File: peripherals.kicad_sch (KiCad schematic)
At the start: 21 parts, among them IC5 MAX11613EUA+T, Q3 BSD235NH6327XTSA1, Q4 BSD235NH6327XTSA1

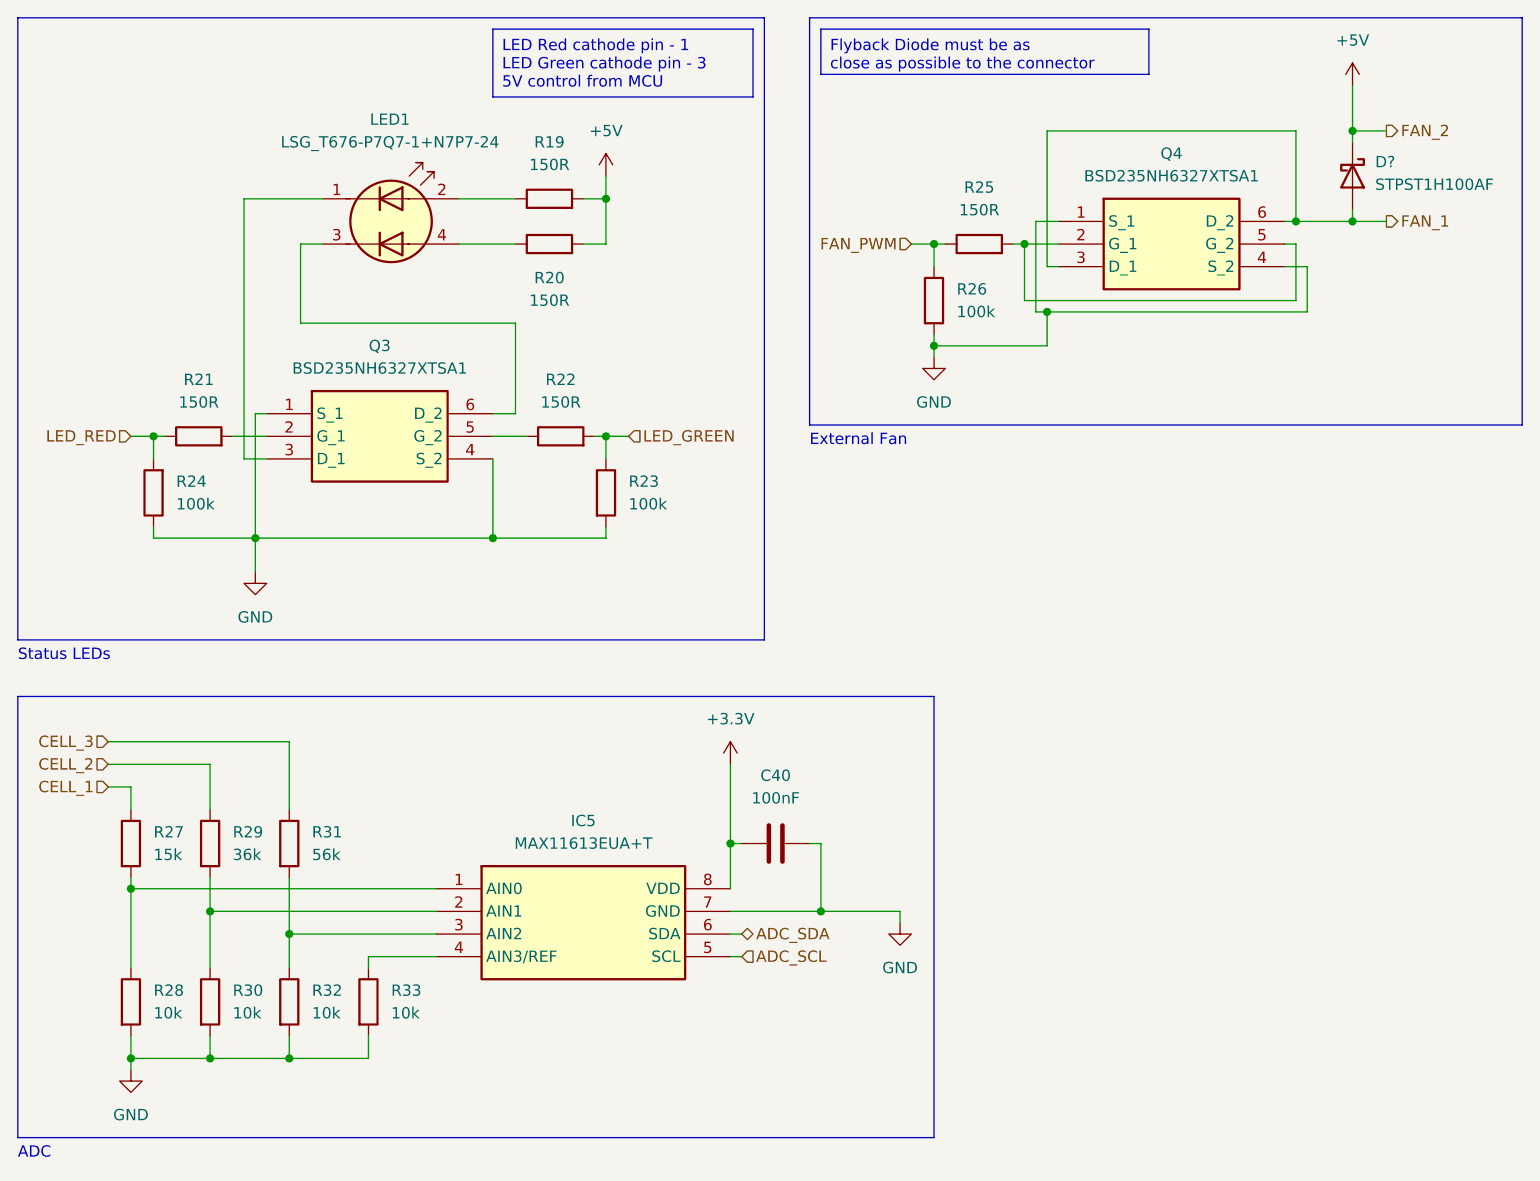
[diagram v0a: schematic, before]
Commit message: New complete schematic version
May need to resize the resistors, also need to change the caps back to electrolytic
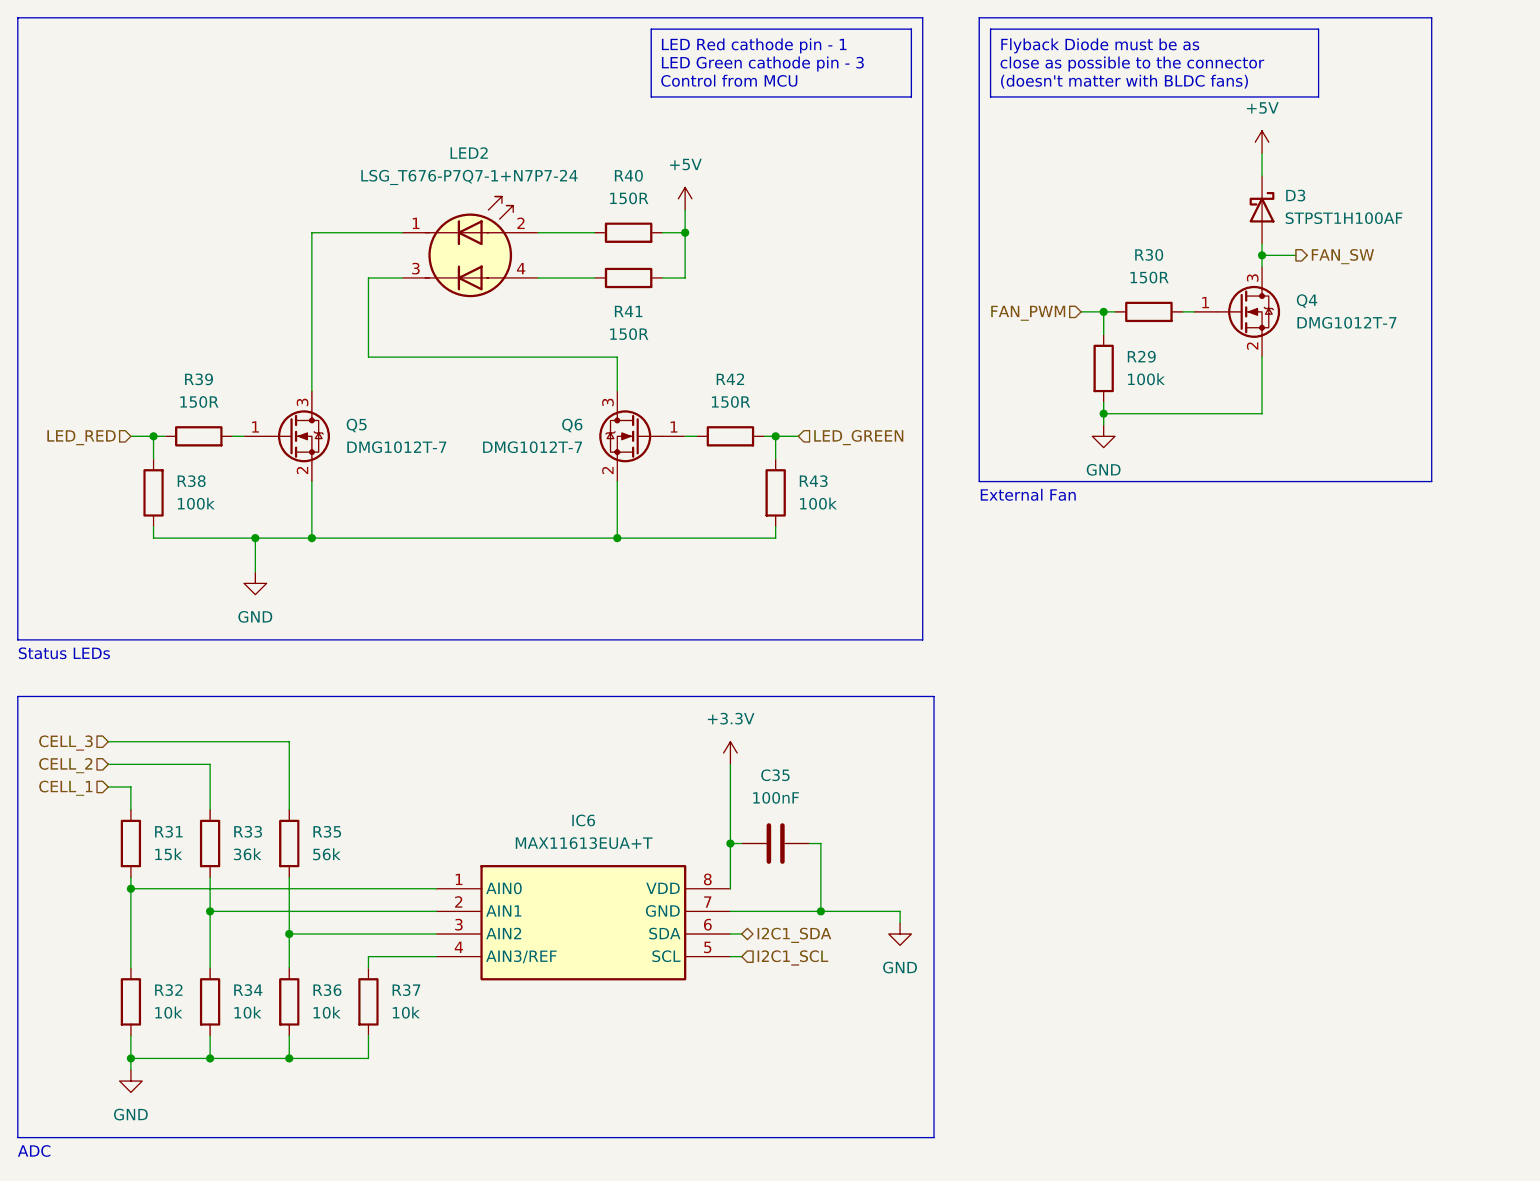
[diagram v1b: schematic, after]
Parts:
- removed Q3, Q4: BSD235NH6327XTSA1, SOT65P210X100-6N, symbol parts:BSD235NH6327XTSA1
- added Q4, Q5, Q6: DMG1012T-7, parts:SOT50P160X80-3N, symbol Device:Q_NMOS_GSD
- C35: renamed from C40; footprint (none) -> Capacitor_SMD:C_0603_1608Metric
- IC6: renamed from IC5; footprint SOP65P490X110-8N -> parts:SOP65P490X110-8N
- R29: renamed from R26; footprint (none) -> Resistor_SMD:R_0603_1608Metric
- R30: renamed from R25; footprint (none) -> Resistor_SMD:R_0603_1608Metric
- R31: renamed from R27; footprint (none) -> Resistor_SMD:R_0603_1608Metric
- R32: renamed from R28; footprint (none) -> Resistor_SMD:R_0603_1608Metric
- R33: renamed from R29; footprint (none) -> Resistor_SMD:R_0603_1608Metric
- R34: renamed from R30; footprint (none) -> Resistor_SMD:R_0603_1608Metric
- R35: renamed from R31; footprint (none) -> Resistor_SMD:R_0603_1608Metric
- R36: renamed from R32; footprint (none) -> Resistor_SMD:R_0603_1608Metric
- R37: renamed from R33; footprint (none) -> Resistor_SMD:R_0603_1608Metric
- R38: renamed from R24; footprint (none) -> Resistor_SMD:R_0603_1608Metric
- R39: renamed from R21; footprint (none) -> Resistor_SMD:R_0603_1608Metric
- R40: renamed from R19; footprint (none) -> Resistor_SMD:R_0603_1608Metric
- R41: renamed from R20; footprint (none) -> Resistor_SMD:R_0603_1608Metric
- R42: renamed from R22; footprint (none) -> Resistor_SMD:R_0603_1608Metric
- R43: renamed from R23; footprint (none) -> Resistor_SMD:R_0603_1608Metric
- gave numbers to parts that had none: 1
- renumbered LED1 to LED2
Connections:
- net GND: now also Q4.2 (S), Q5.2 (S), Q6.2 (S)
- net at R39.2: now also Q5.1 (G)
- net at LED2.1 (A1): now also Q5.3 (D)
- net at R42.1: now also Q6.1 (G)
- net at LED2.3 (A2): now also Q6.3 (D)
- net at R30.2: now also Q4.1 (G)
- net ADC_SCL renamed I2C1_SCL
- net ADC_SDA renamed I2C1_SDA
- net FAN_1 renamed FAN_SW
- net FAN_SW: now also Q4.3 (D)
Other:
- moved on the sheet: D3, LED2, R29, R30, R40, R41, R42, R43

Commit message: Uploaded all project files, finished PCB design
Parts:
- added C4: 4.7uF, Capacitor_SMD:C_0805_2012Metric, symbol Device:C
- D3: value STPST1H100AF -> BAT54GWX; footprint parts:SODFL4724X103N -> parts:SOD123
- renumbered C35 to C44, Q5 to Q4, Q6 to Q5, Q4 to Q6, R38 to R28, R39 to R29, R40 to R30, R41 to R31, R42 to R32, R43 to R33, R29 to R34, R30 to R35, R31 to R36, R32 to R37, R33 to R38, R34 to R39, R35 to R40, R36 to R41, R37 to R42
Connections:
- net +3.3V: now also C4.1
- net GND: now also C4.2
